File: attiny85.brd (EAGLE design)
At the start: 74.7 x 55.5 mm, 8 parts, among them U1 TINY85-20-DIP

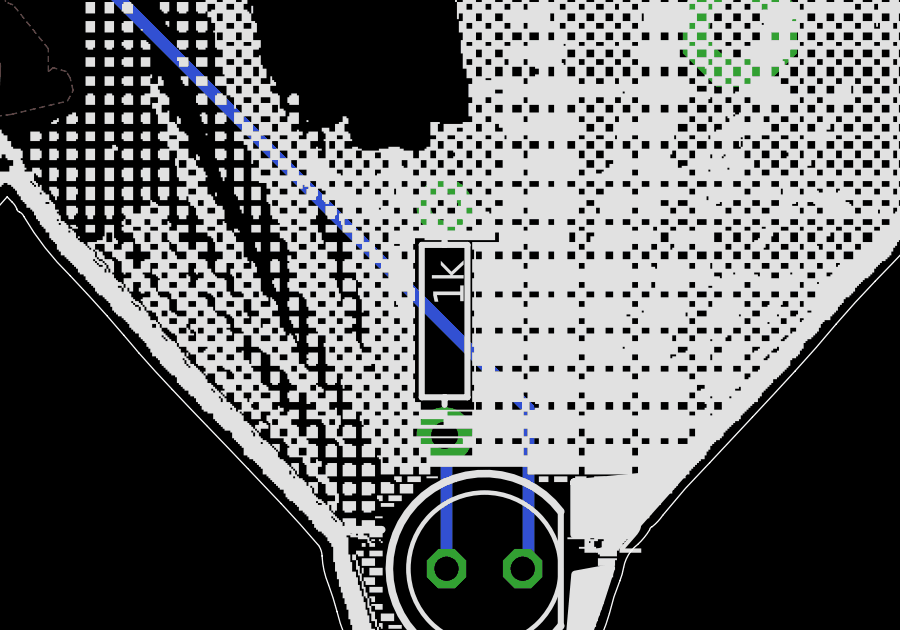
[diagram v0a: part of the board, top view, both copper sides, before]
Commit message: Updating resistor values
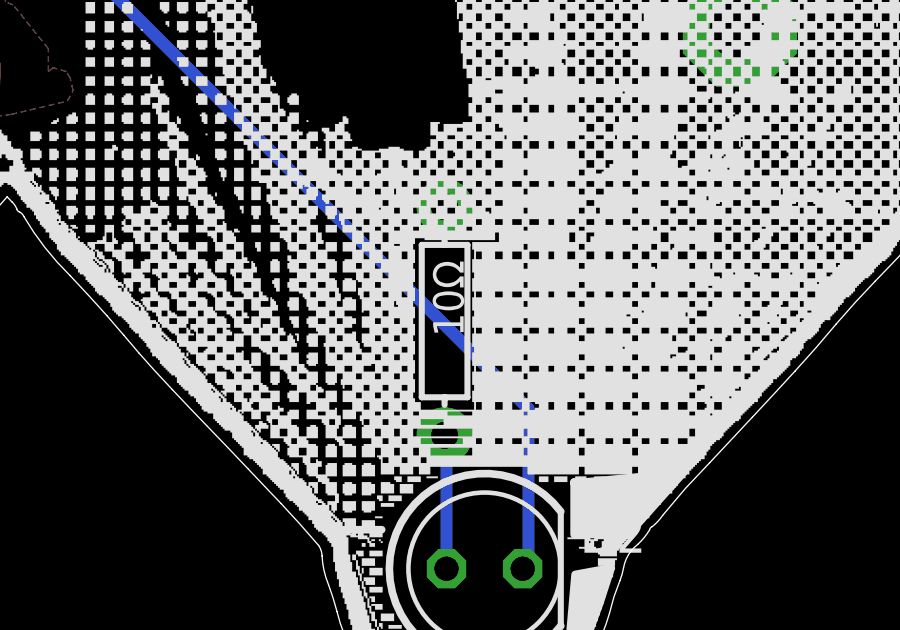
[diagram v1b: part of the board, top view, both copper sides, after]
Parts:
- R2, R3: value 1k -> 10Ω
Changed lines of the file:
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@@
 <attribute name="VALUE" x="17.145" y="40.005" size="0.3048" layer="27" ratio="10" rot="R180"/>
 </element>
-<element name="R2" library="SparkFun-Resistors" package="AXIAL-0.3" value="1k" x="51.816" y="16.891" smashed="yes" rot="R270">
+<element name="R2" library="SparkFun-Resistors" package="AXIAL-0.3" value="10Ω" x="51.816" y="16.891" smashed="yes" rot="R270">
 <attribute name="VALUE" value="1k" x="51.816" y="16.891" size="1.778" layer="27" rot="R270" display="off"/>
 <attribute name="PROD_ID" value="RES-08380" x="51.816" y="16.891" size="1.778" layer="27" rot="R270" display="off"/>
@@
 </element>
 <element name="D2" library="LED" package="LED5MM" value="" x="53.1495" y="8.636"/>
-<element name="R3" library="SparkFun-Resistors" package="AXIAL-0.3" value="1k" x="13.843" y="20.828" rot="R90">
+<element name="R3" library="SparkFun-Resistors" package="AXIAL-0.3" value="10Ω" x="13.843" y="20.828" rot="R90">
 <attribute name="VALUE" value="1k" x="13.843" y="20.828" size="1.778" layer="27" rot="R90" display="off"/>
 <attribute name="PROD_ID" value="RES-08380" x="13.843" y="20.828" size="1.778" layer="27" rot="R90" display="off"/>
